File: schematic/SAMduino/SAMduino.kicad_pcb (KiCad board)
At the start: 4 copper layers, 100 x 100 mm, 97 parts, among them IC1 ATSAMV71N21B-AABT, IC2 MCP1703AT-5002E_CB, IC3 NCP5501DT33RKG, IC4 SST26VF064B-104V_SM, IC5 MCP2221-I_SL, IC6 MCP2542FD-E_SN, J1 Barrel_Jack_Switch, J10 Conn_02x11_Odd_Even, J11 Conn_02x09_Odd_Even, J12 Conn_02x09_Odd_Even, J13 Conn_01x02, J14 Conn_02x02_Odd_Even, J15 Conn_02x03_Odd_Even, J16 Conn_01x02, J17 Conn_02x03_Odd_Even, J18 Conn_02x02_Odd_Even, J19 Conn_02x03_Odd_Even, J2 Conn_02x02_Odd_Even, J20 Conn_01x08, J3 USB_B_Micro, J4 USB_B_Mini, J5 Conn_01x02, J6 Screw_Terminal_01x02, J7 Conn_01x02, J8 Conn_01x02, J9 Conn_02x07_Odd_Even, SW1 SW_MEC_5E, SW2 SW_MEC_5E, SW3 MCLR, SW4 ERASE, X1 AMPMAFB-12.0000T, X2 32.768 kHz 12.5 pF

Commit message: Minor PCB improvements
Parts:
- moved C2 0.48 mm to (67.7, 110.7)
- moved C3 0.48 mm to (67.7, 112.2)
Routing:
- net GND: track 117.5 -> 107.4 mm

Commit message: Minor fixes to PCB
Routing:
- net NRST: track 85.6 -> 80.5 mm
- net ERASE: track 50.3 -> 49.4 mm

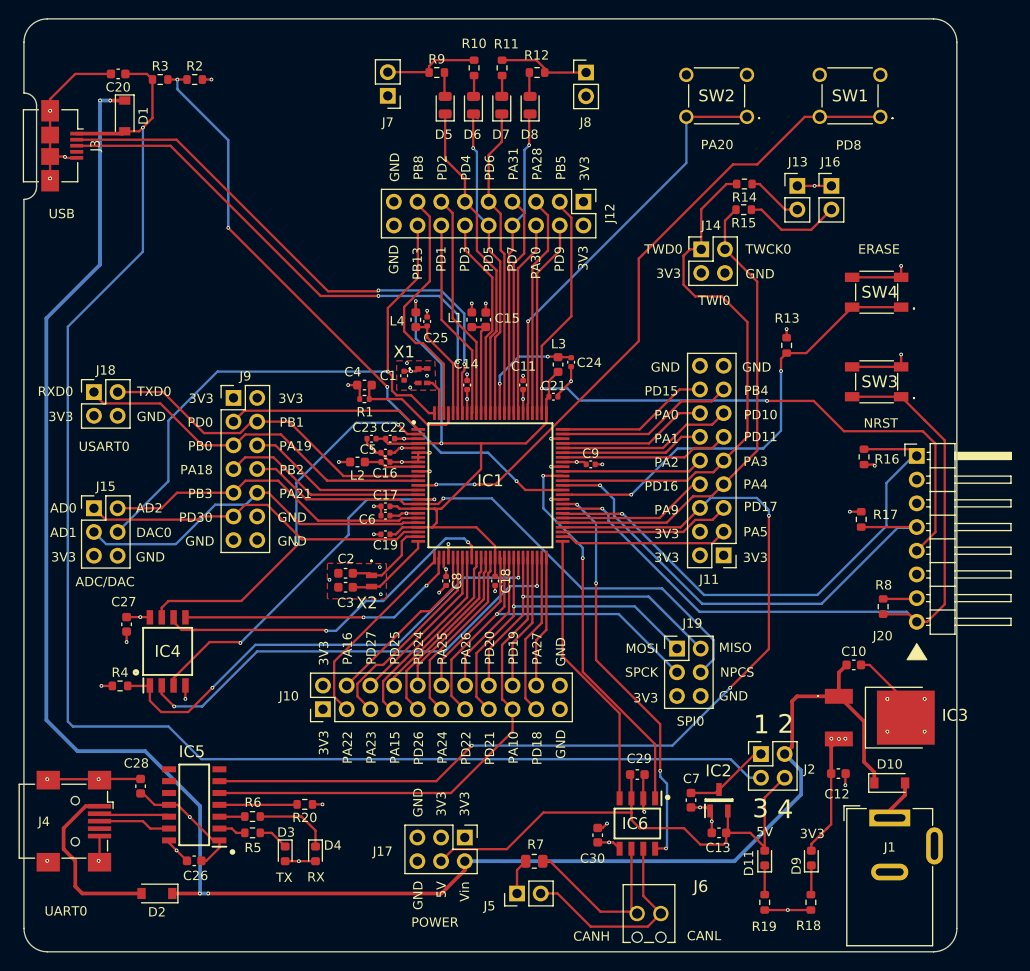
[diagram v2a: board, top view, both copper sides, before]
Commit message: Changed oscillator to 3.2x2.5 size
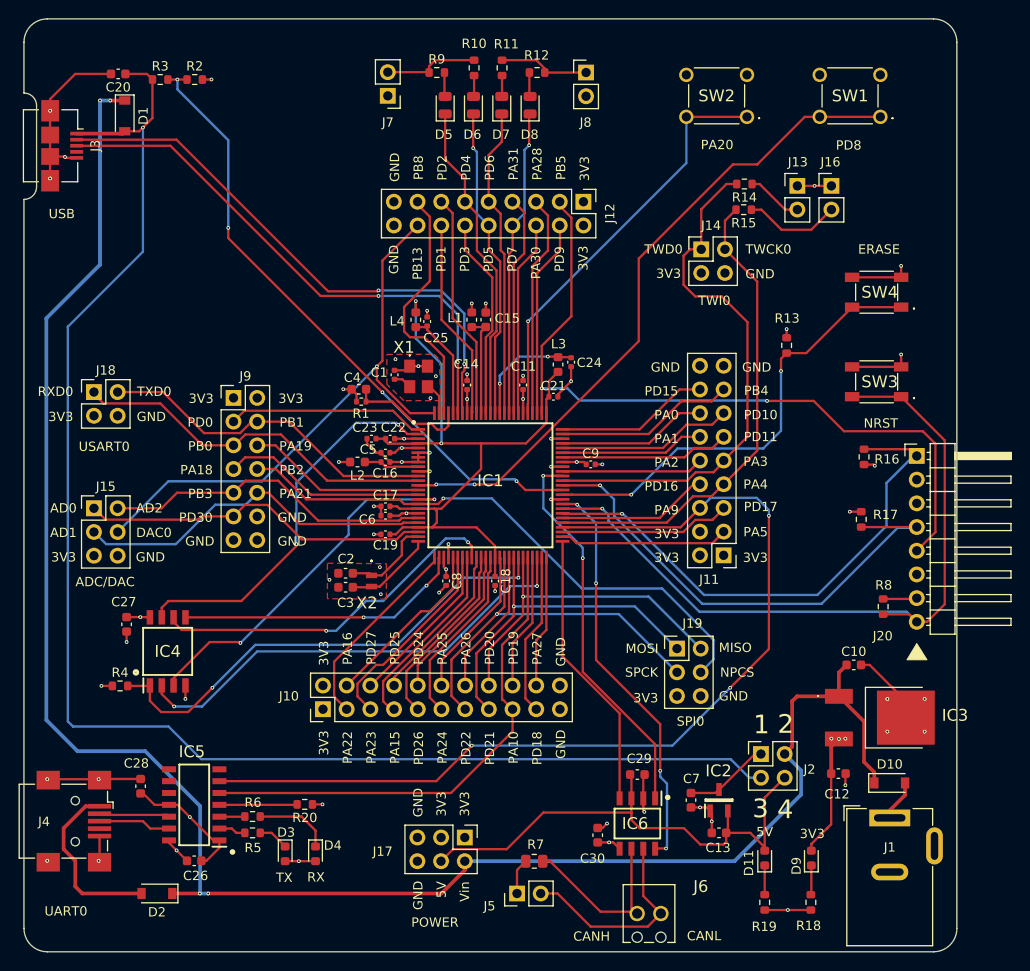
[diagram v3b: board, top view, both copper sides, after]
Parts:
- X1: value AMPMAFB-12.0000T -> 12 MHz; footprint SamacSys_Parts:AMPMAFB120000T -> SamacSys_Parts:ASTMUPCE3312000MHZLJET
- moved C1 1.03 mm to (73.0, 89.4)
- moved C4 0.75 mm to (69.2, 91.0)
- moved X1 0.46 mm to (75.5, 89.6)
- moved R1 0.44 mm to (69.4, 92.3)
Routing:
- net DAC0: track 64.7 -> 61.2 mm
- net VCC3V3: track 74.9 -> 76.1 mm
- net GND: track 107.4 -> 108.5 mm
- net PD5: track 34.2 -> 33.5 mm
- net Net-(C4-Pad1): track 12.3 -> 12.9 mm
- net XIN: track 4.09 -> 3.50 mm
